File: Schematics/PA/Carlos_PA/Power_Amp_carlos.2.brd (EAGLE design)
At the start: 83.5 x 71.1 mm, 105 parts, among them J1 4_PIN_AMPCONN, U1 LME49830, U2 LME49830, U3 LME49830

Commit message: finished my PA board
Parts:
- removed C55: 1984659, Amplifier_Parts:1984659
- added U$6, U$7, U$8: 2TERMINAL_SPEAKER, Amplifier_Parts:2TERMINAL_SPEAKER
- C47, C48, C49, C50, C51, C52: value 1984620 -> OSTVN03A150; device Amplifier_Parts:1984620 -> Amplifier_Parts:OSTVN03A150
- moved C45 129.6 mm to (26.4, 21.6), turned to 270 degrees
- moved C52 129.5 mm to (80.0, 14.6), turned to 180 degrees
- moved C50 127.3 mm to (66.7, 41.6), turned to 270 degrees
- moved C54 123.7 mm to (49.5, 12.4), turned to 180 degrees
- moved R23 123.6 mm to (30.2, 19.1), turned to 180 degrees
- moved VR5 123.3 mm to (35.2, 8.57)
- moved C53 122.5 mm to (41.9, 22.9)
- moved C51 121.9 mm to (69.5, 23.2), turned to 270 degrees
- moved C41 120.9 mm to (26.4, 9.53), turned to 180 degrees
- moved C47 118.7 mm to (70.8, 65.1), turned to 270 degrees
- moved R22 116.1 mm to (20.0, 25.7)
- moved VR6 115.3 mm to (38.4, 8.57)
- moved C48 113.4 mm to (56.5, 58.7), turned to 270 degrees
- moved U3 113.1 mm to (27.9, 17.5), turned to 270 degrees
- moved R21 113.1 mm to (20.3, 21.0)
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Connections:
- net GND: now also U$6.P$2, U$7.P$2, U$8.P$2; no longer C55.P$2, C55.P$4, C55.P$6
- net N$12: now also U$7.P$1; no longer C55.P$3
- net N$75: now also U$6.P$1; no longer C55.P$1
- net N$77: now also U$8.P$1; no longer C55.P$5
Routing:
- net V-: track 121.6 -> 303.5 mm
- net V+: track 128.7 -> 264.7 mm
- net N$77: track 0.00 -> 95.3 mm
- net N$12: track 0.00 -> 78.3 mm, vias 0 -> 4
- net N$75: track 0.00 -> 76.8 mm
- net MUTE: track 0.00 -> 51.9 mm, vias 0 -> 1
- net N$32: track 0.00 -> 35.5 mm
- net N$4: track 0.00 -> 33.1 mm
- net N$15: track 0.00 -> 30.2 mm
- net RIGHT: track 0.00 -> 29.8 mm
- net N$24: track 0.00 -> 28.0 mm, vias 0 -> 1
- net N$30: track 0.00 -> 27.8 mm
- net N$26: track 0.00 -> 27.1 mm
- net N$85: track 0.00 -> 26.7 mm
- net N$42: track 0.00 -> 26.4 mm
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- added copper zone on layer 1, net GND
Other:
- board size 83.5 x 71.1 mm -> 70.2 x 70.2 mm

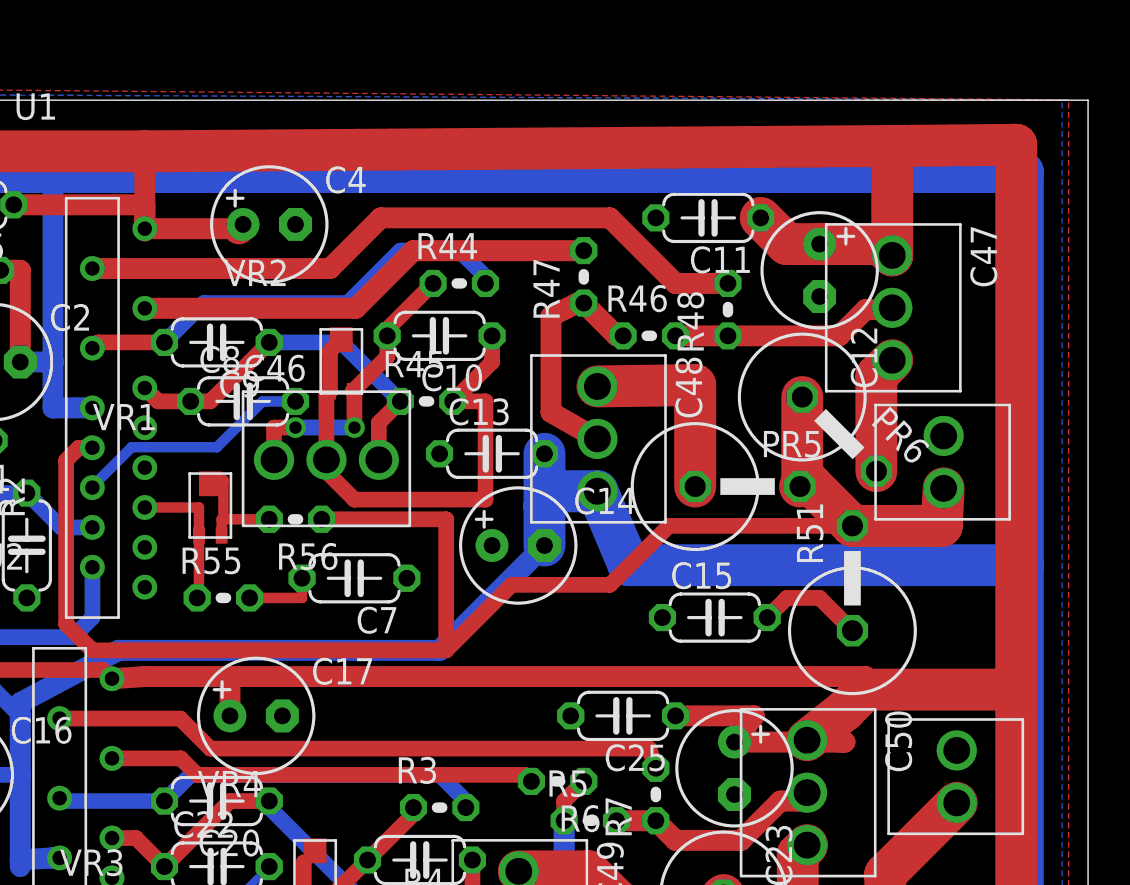
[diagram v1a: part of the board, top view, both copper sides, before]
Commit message: added tstop to big traces, still need some changes to footprints
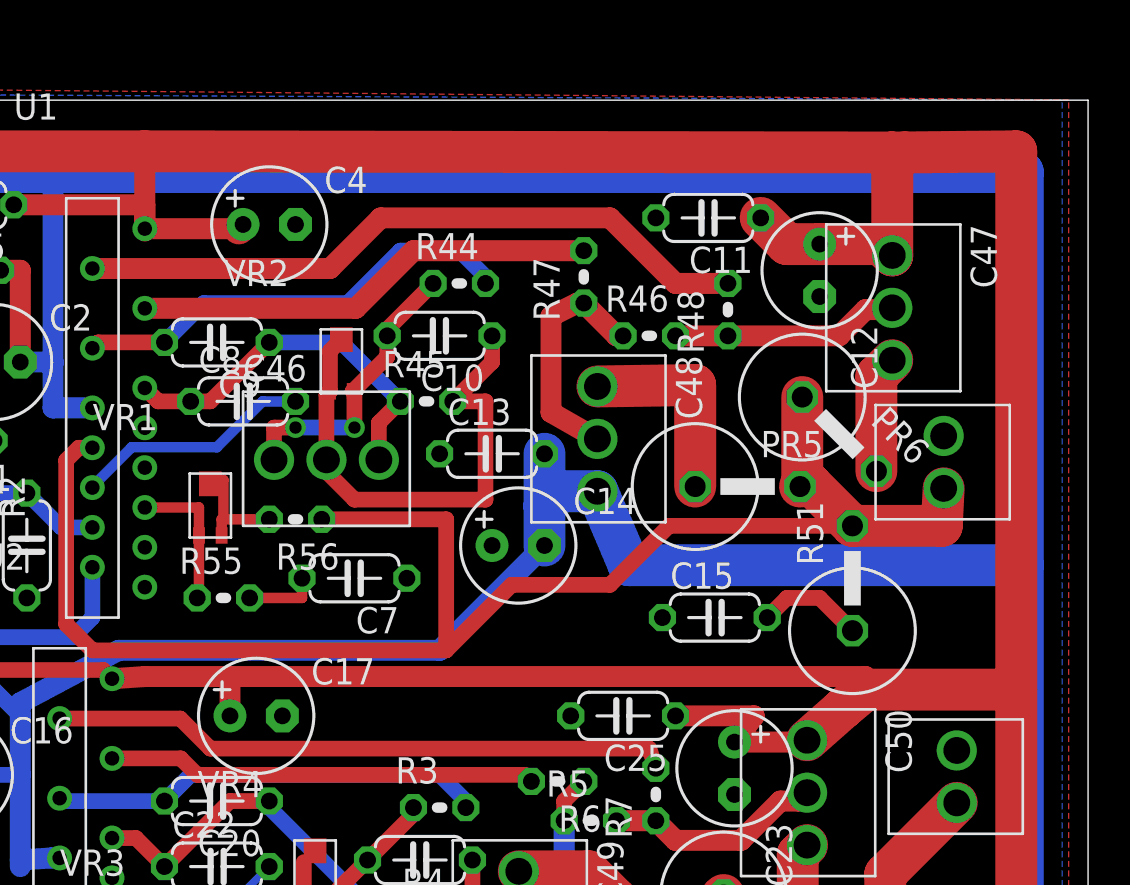
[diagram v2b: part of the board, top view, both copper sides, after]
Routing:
- net V+: track 264.7 -> 260.4 mm
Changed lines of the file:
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@@
 <setting verticaltext="up"/>
 </settings>
-<grid distance="0.0125" unitdist="inch" unit="inch" style="lines" multiple="1" display="no" altdistance="0.025" altunitdist="inch" altunit="inch"/>
+<grid distance="0.003125" unitdist="mic" unit="inch" style="lines" multiple="1" display="no" altdistance="0.025" altunitdist="inch" altunit="inch"/>
 <layers>
 <layer number="1" name="Top" color="4" fill="1" visible="yes" active="yes"/>
@@
 <layer number="27" name="tValues" color="7" fill="1" visible="no" active="yes"/>
 <layer number="28" name="bValues" color="7" fill="1" visible="no" active="yes"/>
-<layer number="29" name="tStop" color="7" fill="3" visible="no" active="yes"/>
+<layer number="29" name="tStop" color="7" fill="3" visible="yes" active="yes"/>
 <layer number="30" name="bStop" color="7" fill="6" visible="no" active="yes"/>
 <layer number="31" name="tCream" color="7" fill="4" visible="no" active="yes"/>
@@
 <wire x1="83.49" y1="71.11" x2="13.335" y2="71.11" width="0" layer="20"/>
 <wire x1="13.335" y1="71.11" x2="13.335" y2="0.9525" width="0" layer="20"/>
+<rectangle x1="78.4225" y1="22.5425" x2="81.28" y2="69.85" layer="29"/>
+<rectangle x1="69.85" y1="41.5925" x2="79.0575" y2="43.815" layer="29"/>
+<rectangle x1="72.80375625" y1="63.19601875" x2="75.151375" y2="67.725803125" layer="29"/>
+<rectangle x1="69.4342375" y1="62.9198125" x2="73.21804375" y2="65.239946875" layer="29"/>
+<rectangle x1="67.252334375" y1="64.07988125" x2="70.2351875" y2="65.626634375" layer="29"/>
+<rectangle x1="67.473284375" y1="63.776053125" x2="69.793284375" y2="64.328465625" layer="29"/>
+<rectangle x1="67.915190625" y1="63.334121875" x2="69.765665625" y2="63.776053125" layer="29"/>
+<rectangle x1="68.46756875" y1="63.030296875" x2="69.68280625" y2="63.416984375" layer="29"/>
+<rectangle x1="68.219" y1="63.057915625" x2="68.660903125" y2="63.5550875" layer="29"/>
+<rectangle x1="72.217296875" y1="52.06151875" x2="74.325334375" y2="57.9103625" layer="29"/>
+<rectangle x1="68.57923125" y1="52.57159375" x2="70.67026875" y2="56.278128125" layer="29"/>
+<rectangle x1="72.504221875" y1="49.45601875" x2="77.120915625" y2="51.602575" layer="29"/>
+<rectangle x1="77.0187" y1="49.77970625" x2="77.46163125" y2="51.755903125" layer="29"/>
+<rectangle x1="70.017" y1="49.95006875" x2="72.998259375" y2="53.101759375" layer="29"/>
+<rectangle x1="69.557034375" y1="50.90409375" x2="70.425859375" y2="51.70479375" layer="29"/>
+<rectangle x1="72.130821875" y1="57.5989" x2="73.477046875" y2="59.02608125" layer="29"/>
+<rectangle x1="63.156628125" y1="52.814503125" x2="65.832525" y2="58.358115625" layer="29"/>
+<rectangle x1="74.430225" y1="32.636228125" x2="76.49473125" y2="38.150915625" layer="29" rot="R135"/>
+<rectangle x1="71.11945625" y1="24.99135" x2="73.1839625" y2="30.5060375" layer="29" rot="R135"/>
+<rectangle x1="72.630178125" y1="28.6629125" x2="74.725565625" y2="34.182959375" layer="29"/>
+<rectangle x1="64.691325" y1="27.393596875" x2="66.7867125" y2="32.559415625" layer="29"/>
+<rectangle x1="64.8979125" y1="26.7737" x2="70.50528125" y2="27.423115625" layer="29"/>
+<rectangle x1="65.399625" y1="26.330915625" x2="70.56430625" y2="26.7737" layer="29"/>
+<rectangle x1="65.9013375" y1="25.82909375" x2="71.15455625" y2="26.12428125" layer="29"/>
+<rectangle x1="66.225975" y1="25.386309375" x2="71.21358125" y2="26.153803125" layer="29"/>
+<rectangle x1="68.414959375" y1="28.76458125" x2="70.443128125" y2="35.348728125" layer="29"/>
+<rectangle x1="60.189796875" y1="56.237521875" x2="64.920871875" y2="58.267390625" layer="29"/>
+<rectangle x1="69.50355" y1="40.6134375" x2="73.14811875" y2="42.12453125" layer="29" rot="R45"/>
 </plain>
 <attributes>
@@
 <contactref element="C51" pad="P$1"/>
 <wire x1="18.955" y1="68.63" x2="37.7825" y2="68.63" width="2.032" layer="1"/>
-<wire x1="37.7825" y1="68.63" x2="73.972984375" y2="68.8903625" width="2.032" layer="1"/>
-<wire x1="73.972984375" y1="68.8903625" x2="74.60795" y2="68.89493125" width="2.032" layer="1"/>
-<wire x1="74.60795" y1="68.89493125" x2="80.01" y2="68.9475" width="2.032" layer="1"/>
-<wire x1="80.01" y1="68.9475" x2="80.01" y2="42.545" width="2.032" layer="1"/>
+<wire x1="37.7825" y1="68.63" x2="73.972984375" y2="68.5728625" width="2.032" layer="1"/>
+<wire x1="73.972984375" y1="68.5728625" x2="74.60795" y2="68.57743125" width="2.032" layer="1"/>
+<wire x1="74.60795" y1="68.57743125" x2="80.01" y2="68.63" width="2.032" layer="1"/>
+<wire x1="80.01" y1="68.63" x2="80.01" y2="42.545" width="2.032" layer="1"/>
 <wire x1="37.7825" y1="64.8825" x2="37.7825" y2="68.63" width="1.016" layer="1"/>
 <wire x1="37.7825" y1="64.8825" x2="42.34" y2="64.8825" width="1.016" layer="1"/>
@@
 <wire x1="68.8975" y1="64.135" x2="67.6275" y2="65.405" width="2.032" layer="1"/>
 <wire x1="37.7825" y1="64.77" x2="37.7825" y2="64.8825" width="1.016" layer="1"/>
-<wire x1="69.875" y1="40.0925" x2="71.71" y2="41.5475" width="2.032" layer="1"/>
-<wire x1="71.71" y1="41.5475" x2="72.7075" y2="42.545" width="2.032" layer="1"/>
+<wire x1="69.875" y1="40.0925" x2="71.620815625" y2="41.63669375" width="2.032" layer="1"/>
+<wire x1="71.620815625" y1="41.63669375" x2="72.7075" y2="42.545" width="2.032" layer="1"/>
 <wire x1="37.7825" y1="43.18" x2="41.91" y2="43.18" width="1.016" layer="1"/>
 <wire x1="41.91" y1="43.18" x2="72.7075" y2="43.18" width="1.016" layer="1"/>
@@
 <wire x1="63.5" y1="41.275" x2="67.31" y2="41.275" width="1.016" layer="1"/>
 <wire x1="67.31" y1="41.275" x2="66.3575" y2="40.005" width="1.016" layer="1"/>
-<wire x1="66.3575" y1="40.005" x2="71.71" y2="40.005" width="1.016" layer="1"/>
-<wire x1="71.71" y1="40.005" x2="69.875" y2="40.0925" width="1.016" layer="1"/>
+<wire x1="66.3575" y1="40.005" x2="69.842421875" y2="40.005" width="1.016" layer="1"/>
+<wire x1="69.842421875" y1="40.005" x2="69.875" y2="40.0925" width="1.016" layer="1"/>
 <wire x1="41.91" y1="41.275" x2="41.91" y2="43.18" width="1.016" layer="1"/>
 <wire x1="31.4325" y1="66.04" x2="37.7825" y2="66.04" width="1.016" layer="1"/>
@@
 <wire x1="70.485" y1="64.135" x2="73.455" y2="64.135" width="2.032" layer="1"/>
 <wire x1="73.455" y1="64.135" x2="74.0025" y2="63.5875" width="2.032" layer="1"/>
-<wire x1="74.0025" y1="63.5875" x2="74.0025" y2="68.860846875" width="2.032" layer="1"/>
-<wire x1="74.0025" y1="68.860846875" x2="73.972984375" y2="68.8903625" width="2.032" layer="1"/>
+<wire x1="74.0025" y1="63.5875" x2="74.0025" y2="68.543346875" width="2.032" layer="1"/>
+<wire x1="74.0025" y1="68.543346875" x2="73.972984375" y2="68.5728625" width="2.032" layer="1"/>
 <wire x1="36.625" y1="12.3825" x2="36.625" y2="13.4475" width="0.762" layer="1"/>
 <wire x1="36.625" y1="13.4475" x2="39.37" y2="16.1925" width="0.762" layer="1"/>

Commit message: updating to master
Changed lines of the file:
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@@
 <setting verticaltext="up"/>
 </settings>
-<grid distance="0.003125" unitdist="mic" unit="inch" style="lines" multiple="1" display="no" altdistance="0.025" altunitdist="inch" altunit="inch"/>
+<grid distance="0.01" unitdist="inch" unit="inch" style="lines" multiple="1" display="yes" altdistance="0.025" altunitdist="inch" altunit="inch"/>
 <layers>
-<layer number="1" name="Top" color="4" fill="1" visible="yes" active="yes"/>
+<layer number="1" name="Top" color="4" fill="1" visible="no" active="yes"/>
 <layer number="16" name="Bottom" color="1" fill="1" visible="yes" active="yes"/>
 <layer number="17" name="Pads" color="2" fill="1" visible="yes" active="yes"/>
@@
 <layer number="19" name="Unrouted" color="6" fill="1" visible="yes" active="yes"/>
 <layer number="20" name="Dimension" color="15" fill="1" visible="yes" active="yes"/>
-<layer number="21" name="tPlace" color="7" fill="1" visible="yes" active="yes"/>
+<layer number="21" name="tPlace" color="7" fill="1" visible="no" active="yes"/>
 <layer number="22" name="bPlace" color="7" fill="1" visible="yes" active="yes"/>
 <layer number="23" name="tOrigins" color="15" fill="1" visible="yes" active="yes"/>
 <layer number="24" name="bOrigins" color="15" fill="1" visible="yes" active="yes"/>
-<layer number="25" name="tNames" color="7" fill="1" visible="yes" active="yes"/>
+<layer number="25" name="tNames" color="7" fill="1" visible="no" active="yes"/>
 <layer number="26" name="bNames" color="7" fill="1" visible="yes" active="yes"/>
 <layer number="27" name="tValues" color="7" fill="1" visible="no" active="yes"/>
@@
 </class>
 </classes>
-<designrules name="default">
-<description language="de">&lt;b&gt;EAGLE Design Rules&lt;/b&gt;
+<designrules name="epl-lpkf">
+<description language="en">&lt;b&gt;EAGLE Design Rules for PSU Electronics Prototyping Lab&lt;/b&gt;
 &lt;p&gt;
-Die Standard-Design-Rules sind so gewählt, dass sie für
-die meisten Anwendungen passen. Sollte ihre Platine
-besondere Anforderungen haben, treffen Sie die erforderlichen
-Einstellungen hier und speichern die Design Rules unter
-einem neuen Namen ab.</description>
-<description language="en">&lt;b&gt;EAGLE Design Rules&lt;/b&gt;
-&lt;p&gt;
-The default Design Rules have been set to cover
-a wide range of applications. Your particular design
-may have different requirements, so please make the
-necessary adjustments and save your customized
-design rules under a new name.</description>
+2013-03-03: Modified from  &lt;b&gt;sunstone_quickturn.dru&lt;/b&gt; to meet minimum drills and spacing for the LPKF S63 Circuit Board Router.
+&lt;/p&gt;</description>
 <param name="layerSetup" value="(1*16)"/>
-<param name="mtCopper" value="0.035mm 0.035mm 0.035mm 0.035mm 0.035mm 0.035mm 0.035mm 0.035mm 0.035mm 0.035mm 0.035mm 0.035mm 0.035mm 0.035mm 0.035mm 0.035mm"/>
-<param name="mtIsolate" value="1.5mm 0.15mm 0.2mm 0.15mm 0.2mm 0.15mm 0.2mm 0.15mm 0.2mm 0.15mm 0.2mm 0.15mm 0.2mm 0.15mm 0.2mm"/>
+<param name="mtCopper" value="0.0178mm 0.0356mm 0.0356mm 0.0356mm 0.0356mm 0.0356mm 0.0356mm 0.0356mm 0.0356mm 0.0356mm 0.0356mm 0.0356mm 0.0356mm 0.0356mm 0.0356mm 0.0178mm"/>
+<param name="mtIsolate" value="59mil 0.1499mm 0.2007mm 0.1499mm 0.2007mm 0.1499mm 0.2007mm 0.1499mm 0.2007mm 0.1499mm 0.2007mm 0.1499mm 0.2007mm 0.1499mm 0.2007mm"/>
 <param name="mdWireWire" value="8mil"/>
 <param name="mdWirePad" value="8mil"/>
@@
 <param name="mdViaViaSameLayer" value="8mil"/>
 <param name="mnLayersViaInSmd" value="2"/>
-<param name="mdCopperDimension" value="40mil"/>
-<param name="mdDrill" value="8mil"/>
+<param name="mdCopperDimension" value="15mil"/>
+<param name="mdDrill" value="15mil"/>
 <param name="mdSmdStop" value="0mil"/>
-<param name="msWidth" value="10mil"/>
-<param name="msDrill" value="24mil"/>
-<param name="msMicroVia" value="9.99mm"/>
+<param name="msWidth" value="8mil"/>
+<param name="msDrill" value="0.35mm"/>
+<param name="msMicroVia" value="9.9898mm"/>
 <param name="msBlindViaRatio" value="0.5"/>
 <param name="rvPadTop" value="0.25"/>
@@
 <param name="rvMicroViaOuter" value="0.25"/>
 <param name="rvMicroViaInner" value="0.25"/>
-<param name="rlMinPadTop" value="10mil"/>
-<param name="rlMaxPadTop" value="20mil"/>
-<param name="rlMinPadInner" value="10mil"/>
-<param name="rlMaxPadInner" value="20mil"/>
-<param name="rlMinPadBottom" value="10mil"/>
-<param name="rlMaxPadBottom" value="20mil"/>
+<param name="rlMinPadTop" value="8mil"/>
+<param name="rlMaxPadTop" value="999mil"/>
+<param name="rlMinPadInner" value="0mil"/>
+<param name="rlMaxPadInner" value="0mil"/>
+<param name="rlMinPadBottom" value="8mil"/>
+<param name="rlMaxPadBottom" value="999mil"/>
 <param name="rlMinViaOuter" value="8mil"/>
-<param name="rlMaxViaOuter" value="20mil"/>
-<param name="rlMinViaInner" value="8mil"/>
-<param name="rlMaxViaInner" value="20mil"/>
-<param name="rlMinMicroViaOuter" value="4mil"/>
-<param name="rlMaxMicroViaOuter" value="20mil"/>
-<param name="rlMinMicroViaInner" value="4mil"/>
-<param name="rlMaxMicroViaInner" value="20mil"/>
+<param name="rlMaxViaOuter" value="999mil"/>
+<param name="rlMinViaInner" value="0mil"/>
+<param name="rlMaxViaInner" value="0mil"/>
+<param name="rlMinMicroViaOuter" value="8mil"/>
+<param name="rlMaxMicroViaOuter" value="999mil"/>
+<param name="rlMinMicroViaInner" value="0mil"/>
+<param name="rlMaxMicroViaInner" value="0mil"/>
 <param name="psTop" value="-1"/>
 <param name="psBottom" value="-1"/>
@@
 <param name="mvStopFrame" value="1"/>
 <param name="mvCreamFrame" value="0"/>
-<param name="mlMinStopFrame" value="4mil"/>
-<param name="mlMaxStopFrame" value="4mil"/>
+<param name="mlMinStopFrame" value="3mil"/>
+<param name="mlMaxStopFrame" value="3mil"/>
 <param name="mlMinCreamFrame" value="0mil"/>
 <param name="mlMaxCreamFrame" value="0mil"/>
@@
 <param name="checkRestrict" value="1"/>
 <param name="useDiameter" value="13"/>
-<param name="maxErrors" value="50"/>
+<param name="maxErrors" value="500"/>
 </designrules>
 <autorouter>
@@
 <contactref element="U$7" pad="P$2"/>
 <contactref element="U$8" pad="P$2"/>
-<wire x1="21.185" y1="12.3825" x2="21.59" y2="20.955" width="0" layer="19" extent="1-1"/>
 </signal>
 <signal name="V-">

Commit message: Finished My PA and made changes to Carlos' PA
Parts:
- removed C46, C47, C48, C49, C50, C51, C52, C53, C54: OSTVN03A150, Amplifier_Parts:OSTVN03A150
- removed U$5: SCREW_TERMINAL_4, Amplifier_Parts:SCREW_TERMINAL_4
- removed U$6, U$7, U$8: 2TERMINAL_SPEAKER, Amplifier_Parts:2TERMINAL_SPEAKER
- added J10, J11, J12, J13, J14, J6, J7, J8, J9: OSTVN03A150, Amplifier_Parts:OSTVN03A150
- added J2: 1984633, Amplifier_Parts:1984633
- added J3, J4, J5: 2TERMINAL_SPEAKER, Amplifier_Parts:2TERMINAL_SPEAKER
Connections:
- net GND: now also J2.P$2, J3.P$2, J4.P$2, J5.P$2; no longer U$5.2, U$6.P$2, U$7.P$2, U$8.P$2
- net MUTE: now also J2.P$1; no longer U$5.1
- net N$1: now also J10.P$1; no longer C53.P$1
- net N$11: now also J9.P$3; no longer C50.P$3
- net N$110: now also J8.P$1; no longer C48.P$1
- net N$12: now also J4.P$1; no longer U$7.P$1
- net N$2: now also J10.P$2; no longer C53.P$2
- net N$22: now also J11.P$1; no longer C49.P$1
- net N$23: now also J13.P$1; no longer C54.P$1
- net N$24: now also J13.P$2; no longer C54.P$2
- net N$26: now also J13.P$3; no longer C54.P$3
- net N$30: now also J12.P$2; no longer C51.P$2
- net N$32: now also J14.P$2; no longer C52.P$2
- net N$33: now also J12.P$3; no longer C51.P$3
- net N$45: now also J14.P$1; no longer C52.P$1
- net N$5: now also J10.P$3; no longer C53.P$3
- net N$65: now also J7.P$1; no longer C46.P$1
- net N$67: now also J7.P$3; no longer C46.P$3
- net N$68: now also J7.P$2; no longer C46.P$2
- net N$72: now also J6.P$2; no longer C47.P$2
- net N$73: now also J8.P$2; no longer C48.P$2
- net N$74: now also J6.P$3; no longer C47.P$3
- net N$75: now also J3.P$1; no longer U$6.P$1
- net N$77: now also J5.P$1; no longer U$8.P$1
- net N$8: now also J9.P$2; no longer C50.P$2
- net N$9: now also J11.P$2; no longer C49.P$2
- net V+: now also J12.P$1, J2.P$4, J6.P$1, J9.P$1; no longer C47.P$1, C50.P$1, C51.P$1, U$5.4
- net V-: now also J11.P$3, J14.P$3, J2.P$3, J8.P$3; no longer C48.P$3, C49.P$3, C52.P$3, U$5.3
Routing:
- net MUTE: track 51.9 -> 62.2 mm, vias 1 -> 0
- net V+: track 260.4 -> 255.3 mm
- net N$85: track 26.7 -> 22.3 mm
- net V-: track 303.5 -> 300.4 mm
- net N$9: track 8.20 -> 9.98 mm
- net N$5: track 25.8 -> 27.3 mm
- net N$1: track 14.3 -> 15.5 mm, vias 2 -> 1
- net N$65: track 14.1 -> 13.0 mm, vias 2 -> 1
- net N$75: track 76.8 -> 75.7 mm
- net RIGHT: track 29.8 -> 28.9 mm
- net N$37: track 12.6 -> 11.9 mm
- net N$110: track 9.66 -> 8.98 mm
- net N$73: track 11.5 -> 12.2 mm
- net N$2: track 21.0 -> 21.3 mm, vias 0 -> 1
